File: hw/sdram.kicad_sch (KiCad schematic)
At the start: 23 parts, among them U15 T20Q144xx, U17 NDS36PT5-16ET

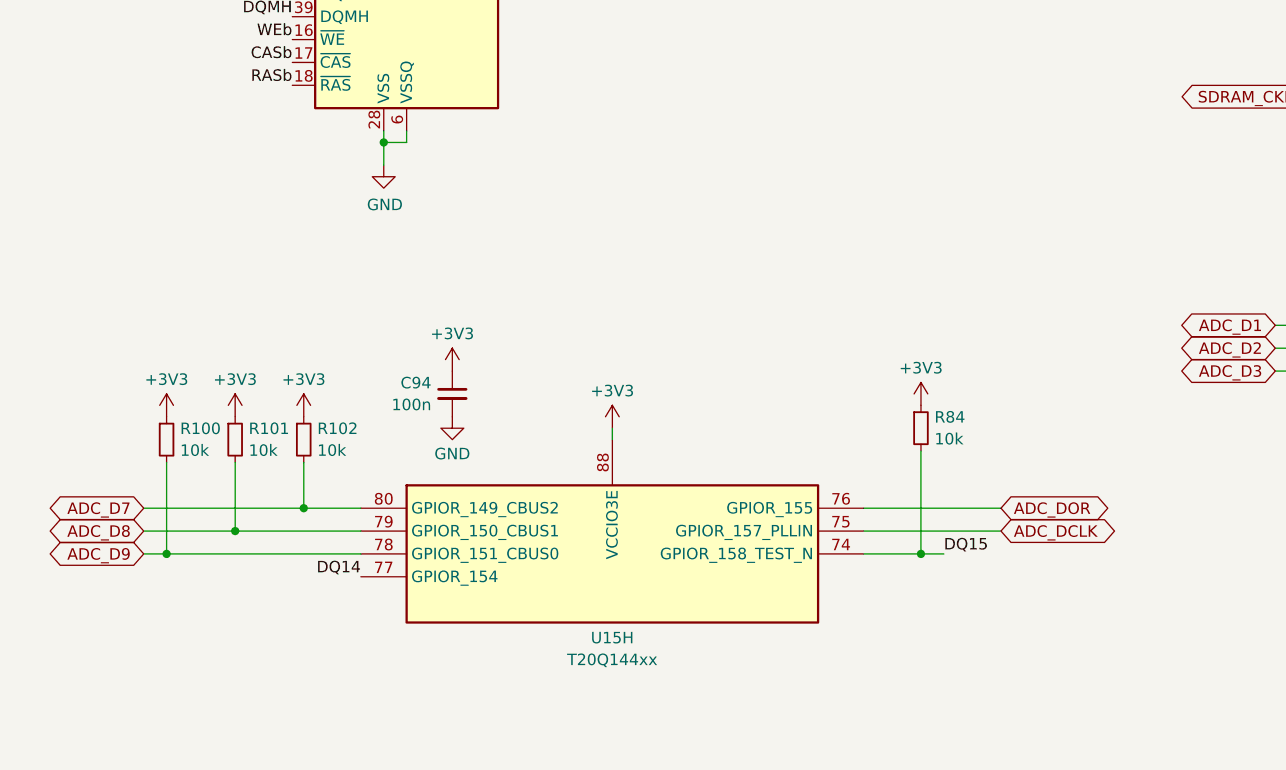
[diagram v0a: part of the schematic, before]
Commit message: Modified DAC resistors/range; connect + pull-up ADC SHDN
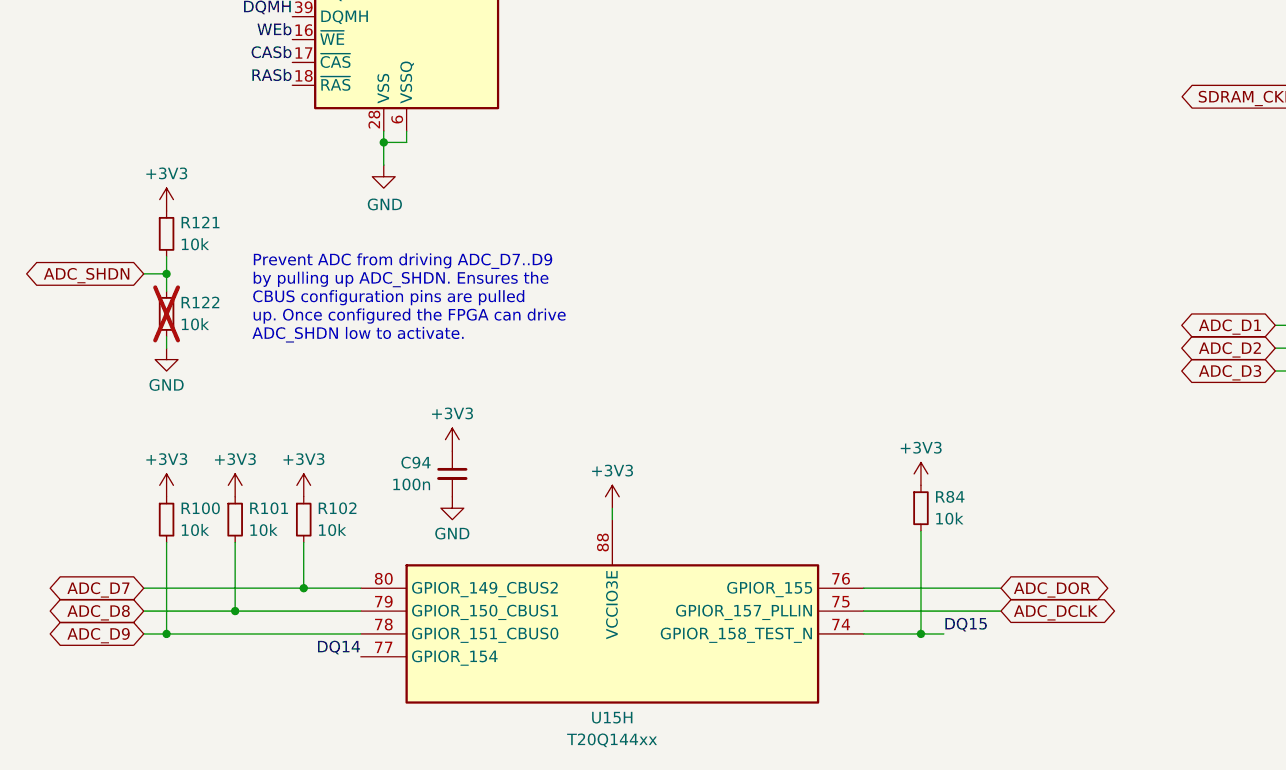
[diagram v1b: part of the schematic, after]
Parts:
- added R121, R122: 10k, Resistor_SMD:R_0603_1608Metric, symbol Device:R_Small
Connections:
- net +3V3: now also R121.1
- net GND: now also R122.2
- new net ADC_SHDN: R121.2, R122.1
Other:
- note added: "Prevent ADC from driving ADC_D7..D9 by pulling up ADC_SHDN. Ensures the CBUS configuration pins are pulled up. Once configured the FPGA can drive ADC_SHDN low to activate."
- moved on the sheet: C94, R100, R101, R102, R84, U15H

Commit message: updated parts assignments
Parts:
- R100, R101, R102, R121, R122, R83, R84: Manufacturer (none) -> Stackpole; Part (none) -> RMCF0603FT10K0
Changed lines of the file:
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@@
 			)
 		)
+		(property "Manufacturer" "Stackpole"
+			(at 45.72 167.64 0)
+			(effects
+				(font
+					(size 1.27 1.27)
+				)
+				(hide yes)
+			)
+		)
+		(property "Part" "RMCF0603FT10K0"
+			(at 45.72 167.64 0)
+			(effects
+				(font
+					(size 1.27 1.27)
+				)
+				(hide yes)
+			)
+		)
 		(pin "2"
 		)
@@
 			)
 		)
+		(property "Manufacturer" "Stackpole"
+			(at 30.48 167.64 0)
+			(effects
+				(font
+					(size 1.27 1.27)
+				)
+				(hide yes)
+			)
+		)
+		(property "Part" "RMCF0603FT10K0"
+			(at 30.48 167.64 0)
+			(effects
+				(font
+					(size 1.27 1.27)
+				)
+				(hide yes)
+			)
+		)
 		(pin "2"
 		)
@@
 			)
 		)
+		(property "Manufacturer" "Stackpole"
+			(at 30.48 144.78 0)
+			(effects
+				(font
+					(size 1.27 1.27)
+				)
+				(hide yes)
+			)
+		)
+		(property "Part" "RMCF0603FT10K0"
+			(at 30.48 144.78 0)
+			(effects
+				(font
+					(size 1.27 1.27)
+				)
+				(hide yes)
+			)
+		)
 		(pin "2"
 		)
@@
 			)
 		)
+		(property "Manufacturer" "Stackpole"
+			(at 30.48 135.89 0)
+			(effects
+				(font
+					(size 1.27 1.27)
+				)
+				(hide yes)
+			)
+		)
+		(property "Part" "RMCF0603FT10K0"
+			(at 30.48 135.89 0)
+			(effects
+				(font
+					(size 1.27 1.27)
+				)
+				(hide yes)
+			)
+		)
 		(pin "2"
 		)
@@
 			)
 		)
+		(property "Manufacturer" "Stackpole"
+			(at 114.3 166.37 0)
+			(effects
+				(font
+					(size 1.27 1.27)
+				)
+				(hide yes)
+			)
+		)
+		(property "Part" "RMCF0603FT10K0"
+			(at 114.3 166.37 0)
+			(effects
+				(font
+					(size 1.27 1.27)
+				)
+				(hide yes)
+			)
+		)
 		(pin "2"
 		)
@@
 			)
 		)
+		(property "Manufacturer" "Stackpole"
+			(at 38.1 167.64 0)
+			(effects
+				(font
+					(size 1.27 1.27)
+				)
+				(hide yes)
+			)
+		)
+		(property "Part" "RMCF0603FT10K0"
+			(at 38.1 167.64 0)
+			(effects
+				(font
+					(size 1.27 1.27)
+				)
+				(hide yes)
+			)
+		)
 		(pin "2"
 		)
@@
 			(at 25.4 97.155 0)
 			(effects
+				(font
+					(size 1.27 1.27)
+				)
+				(hide yes)
+			)
+		)
+		(property "Manufacturer" "Stackpole"
+			(at 25.4 97.155 0)
+			(effects
+				(font
+					(size 1.27 1.27)
+				)
+				(hide yes)
+			)
+		)
+		(property "Part" "RMCF0603FT10K0"
+			(at 25.4 97.155 0)
+			(effects

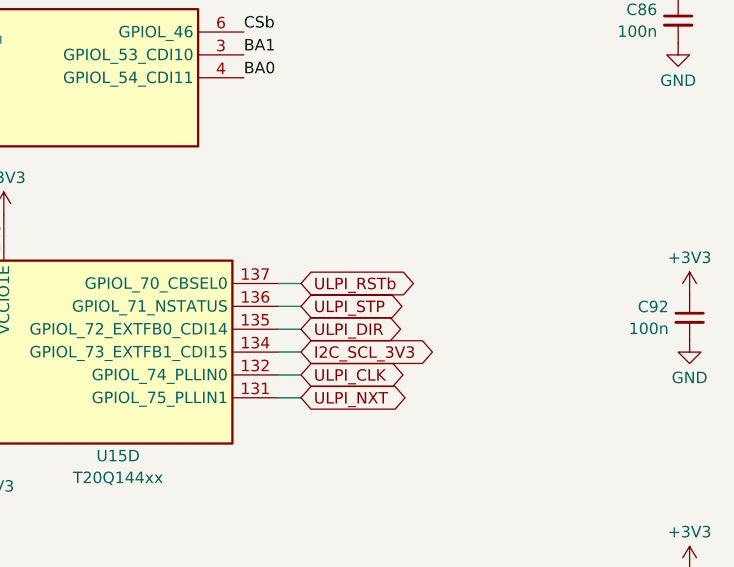
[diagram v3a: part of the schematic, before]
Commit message: connected versaclock CLKSEL to ULPI RSTB (share FPGA pin)
ULPI Rstb is unlikely to be used

Also: - update of kicad to 9.0 (many library footprints updated)
      - added sheet titles, author
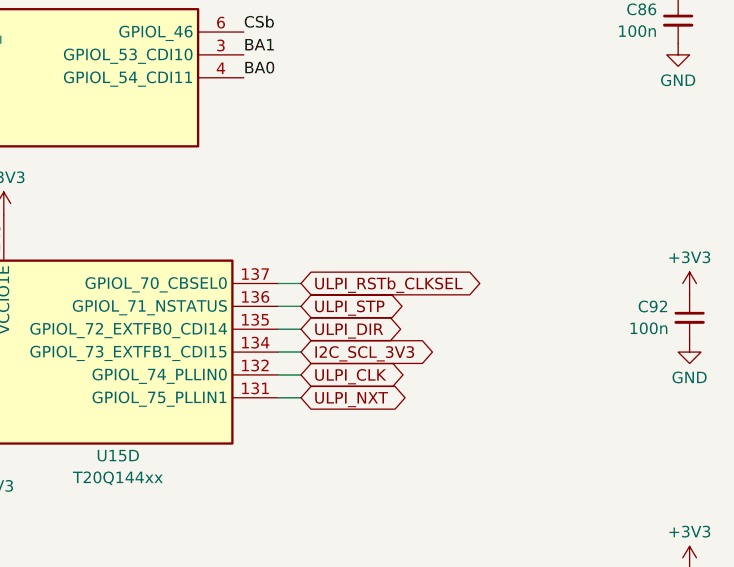
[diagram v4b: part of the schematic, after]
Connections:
- net ULPI_RSTb renamed ULPI_RSTb_CLKSEL
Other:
- company: (none) -> Till Straumann
- title: (none) -> FPGA Bank 1, 3; SDRAM

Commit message: Added licensing information
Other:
- company: Till Straumann -> Copyright Till Straumann, 2025
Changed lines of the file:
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@@
 		(title "FPGA Bank 1, 3; SDRAM")
 		(rev "3.3b")
-		(company "Till Straumann")
+		(company "Copyright Till Straumann, 2025")
+		(comment 1 "License: CERN-OHL-P v2")
 	)
 	(text "Prevent ADC from driving ADC_D7..D9\nby pulling up ADC_SHDN. Ensures the\nCBUS configuration pins are pulled\nup. Once configured the FPGA can drive\nADC_SHDN low to activate."
